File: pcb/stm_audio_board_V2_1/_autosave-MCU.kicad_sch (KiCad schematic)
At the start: 16 parts, among them SW1 SW_SPST, U1 STM32H747IGTx, Y2 X1E0000210132

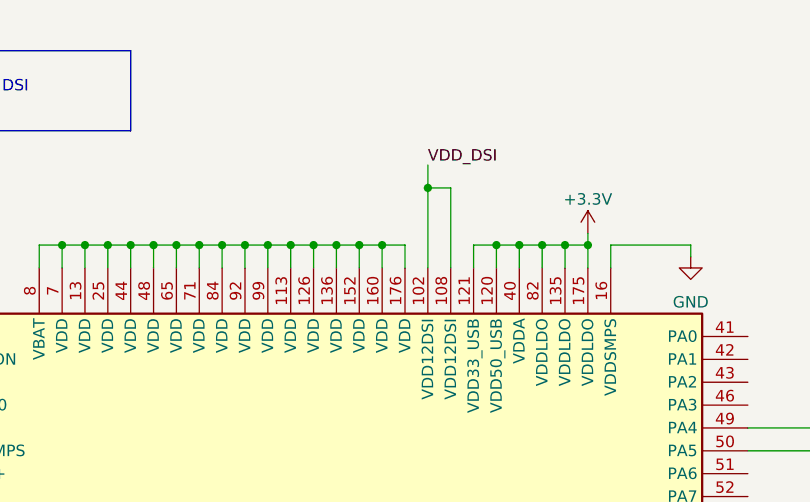
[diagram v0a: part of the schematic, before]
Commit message: input stage is done, fixes for the audioboardV2_1 over
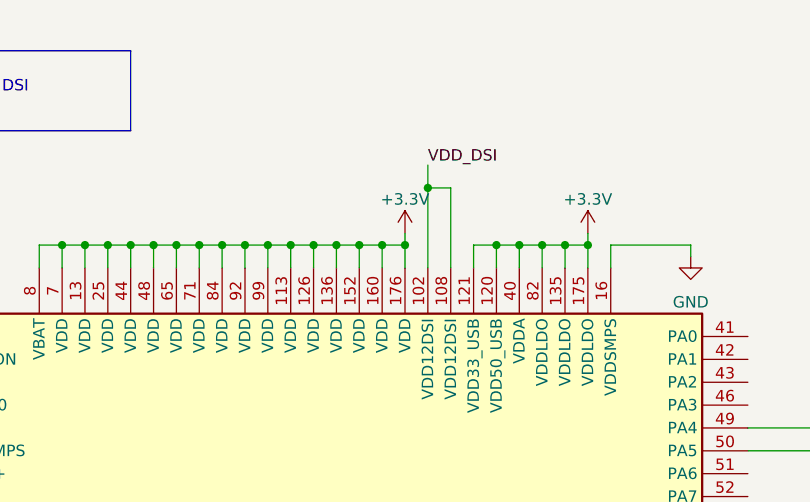
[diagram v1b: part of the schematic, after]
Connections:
- net +3.3V: now also U1.113 (VDD), U1.126 (VDD), U1.13 (VDD), U1.136 (VDD), U1.152 (VDD), U1.160 (VDD), U1.176 (VDD), U1.25 (VDD), U1.44 (VDD), U1.48 (VDD), U1.65 (VDD), U1.7 (VDD), U1.71 (VDD), U1.8 (VBAT), U1.84 (VDD), U1.92 (VDD), U1.99 (VDD)
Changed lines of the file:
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@@
   (junction (at 204.47 40.64) (diameter 0) (color 0 0 0 0)
   )
+  (junction (at 227.33 40.64) (diameter 0) (color 0 0 0 0)
+  )
   (junction (at 201.93 40.64) (diameter 0) (color 0 0 0 0)
   )
@@
   )
   (wire (pts (xy 326.39 77.47) (xy 326.39 76.2))
+    (stroke (width 0) (type default))
+  )
+  (wire (pts (xy 227.33 39.37) (xy 227.33 40.64))
     (stroke (width 0) (type default))
   )
@@
         )
       )
+    )
+  )
+  (symbol (lib_id "power:+3.3V") (at 227.33 39.37 0) (unit 1)
+    (in_bom yes) (on_board yes) (dnp no) (fields_autoplaced)
+    (property "Reference" "#PWR081" (at 227.33 43.18 0)
+      (effects (font (size 1.27 1.27)) hide)
+    )
+    (property "Value" "+3.3V" (at 227.33 35.56 0)
+      (effects (font (size 1.27 1.27)))
+    )
+    (property "Footprint" "" (at 227.33 39.37 0)
+      (effects (font (size 1.27 1.27)) hide)
+    )
+    (property "Datasheet" "" (at 227.33 39.37 0)
+      (effects (font (size 1.27 1.27)) hide)
+    )
+    (pin "1")
+    (instances
+      (project "stm_audio_board_V2_1"
+        (path "/6997cf63-2615-4e49-9471-e7da1b6bae71/2eb2ee8f-ab98-4666-97f0-bfacb073bc88"
+          (reference "#PWR081") (unit 1)
+        )
+        (path "/6997cf63-2615-4e49-9471-e7da1b6bae71/51aec99e-3301-49b6-8e7f-31ba63a05d64"
+          (reference "#PWR057") (unit 1)
+        )
+      )
